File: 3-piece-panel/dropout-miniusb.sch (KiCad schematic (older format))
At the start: 47 parts, among them SW1 Rotary_Encoder_Switch, SW2 SW_Push, U1 ProMicro

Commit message: 3 piece panelization
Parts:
- H1, H2, H3, H4, H5: footprint MountingHole:MountingHole_2.2mm_M2_Pad -> MountingHole:MountingHole_3.7mm
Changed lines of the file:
@@
 F 0 "H2" H 7900 2196 50  0000 L CNN
 F 1 "MountingHole" H 7900 2105 50  0000 L CNN
-F 2 "MountingHole:MountingHole_2.2mm_M2_Pad" H 7800 2150 50  0001 C CNN
+F 2 "MountingHole:MountingHole_3.7mm" H 7800 2150 50  0001 C CNN
 F 3 "~" H 7800 2150 50  0001 C CNN
 	1    7800 2150
@@
 F 0 "H3" H 7900 2546 50  0000 L CNN
 F 1 "MountingHole" H 7900 2455 50  0000 L CNN
-F 2 "MountingHole:MountingHole_2.2mm_M2_Pad" H 7800 2500 50  0001 C CNN
+F 2 "MountingHole:MountingHole_3.7mm" H 7800 2500 50  0001 C CNN
 F 3 "~" H 7800 2500 50  0001 C CNN
 	1    7800 2500
@@
 F 0 "H4" H 7900 2896 50  0000 L CNN
 F 1 "MountingHole" H 7900 2805 50  0000 L CNN
-F 2 "MountingHole:MountingHole_2.2mm_M2_Pad" H 7800 2850 50  0001 C CNN
+F 2 "MountingHole:MountingHole_3.7mm" H 7800 2850 50  0001 C CNN
 F 3 "~" H 7800 2850 50  0001 C CNN
 	1    7800 2850
@@
 F 0 "H5" H 7900 3246 50  0000 L CNN
 F 1 "MountingHole" H 7900 3155 50  0000 L CNN
-F 2 "MountingHole:MountingHole_2.2mm_M2_Pad" H 7800 3200 50  0001 C CNN
+F 2 "MountingHole:MountingHole_3.7mm" H 7800 3200 50  0001 C CNN
 F 3 "~" H 7800 3200 50  0001 C CNN
 	1    7800 3200
@@
 F 0 "H1" H 7900 1896 50  0000 L CNN
 F 1 "MountingHole" H 7900 1805 50  0000 L CNN
-F 2 "MountingHole:MountingHole_2.2mm_M2_Pad" H 7800 1850 50  0001 C CNN
+F 2 "MountingHole:MountingHole_3.7mm" H 7800 1850 50  0001 C CNN
 F 3 "~" H 7800 1850 50  0001 C CNN
 	1    7800 1850

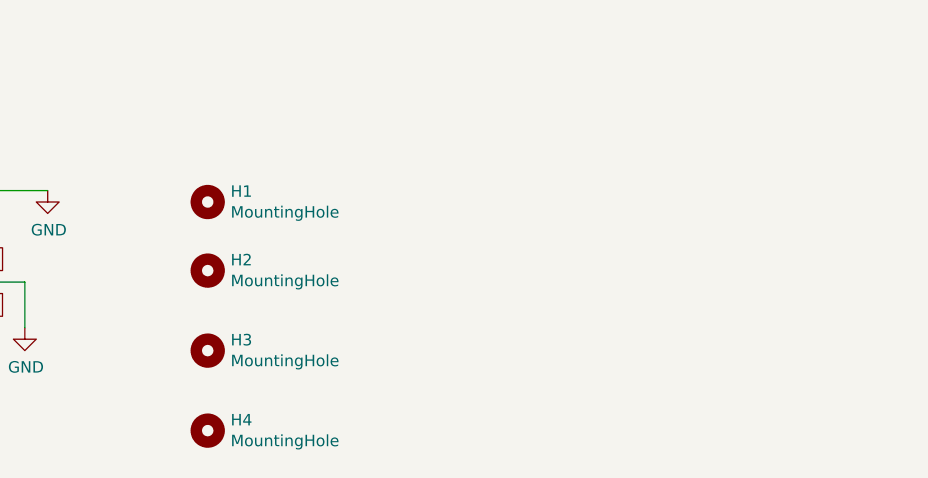
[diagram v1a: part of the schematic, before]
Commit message: adding copper plated mounting holes
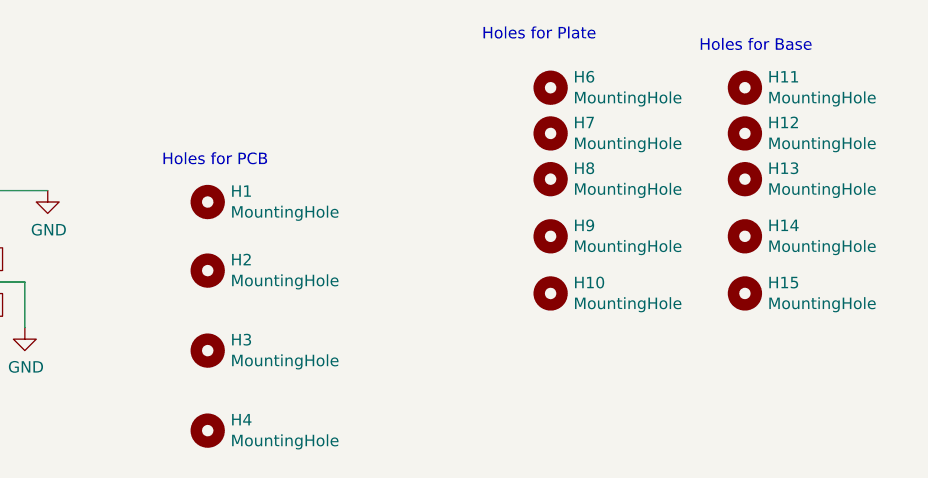
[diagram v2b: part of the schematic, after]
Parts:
- added H10, H11, H12, H13, H14, H15, H6, H7, H8, H9: MountingHole, MountingHole:MountingHole_2.2mm_M2_Pad, symbol Mechanical:MountingHole
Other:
- note added: "Holes for Base"
- note added: "Holes for PCB"
- note added: "Holes for Plate"
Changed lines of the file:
@@
 Wire Wire Line
 	8350 4050 8850 4050
-$Comp
-L power:GND #PWR08
-U 1 1 5FD00893
-P 9300 3750
-F 0 "#PWR08" H 9300 3500 50  0001 C CNN
-F 1 "GND" H 9305 3577 50  0000 C CNN
-F 2 "" H 9300 3750 50  0001 C CNN
-F 3 "" H 9300 3750 50  0001 C CNN
-	1    9300 3750
-	1    0    0    -1
-$EndComp
 Wire Wire Line
 	8850 4050 8850 3900
@@
 	1    0    0    -1
 $EndComp
-Connection ~ 9000 3750
-Wire Wire Line
-	9000 3750 9300 3750
 NoConn ~ 8350 4650
 Wire Wire Line
@@
 Wire Wire Line
 	6550 1800 7100 1800
+$Comp
+L Mechanical:MountingHole H6
+U 1 1 5FCEF804
+P 9300 1350
+F 0 "H6" H 9400 1396 50  0000 L CNN
+F 1 "MountingHole" H 9400 1305 50  0000 L CNN
+F 2 "MountingHole:MountingHole_2.2mm_M2_Pad" H 9300 1350 50  0001 C CNN
+F 3 "~" H 9300 1350 50  0001 C CNN
+	1    9300 1350
+	1    0    0    -1
+$EndComp
+$Comp
+L Mechanical:MountingHole H7
+U 1 1 5FCEFF4E
+P 9300 1550
+F 0 "H7" H 9400 1596 50  0000 L CNN
+F 1 "MountingHole" H 9400 1505 50  0000 L CNN
+F 2 "MountingHole:MountingHole_2.2mm_M2_Pad" H 9300 1550 50  0001 C CNN
+F 3 "~" H 9300 1550 50  0001 C CNN
+	1    9300 1550
+	1    0    0    -1
+$EndComp
+$Comp
+L Mechanical:MountingHole H8
+U 1 1 5FCF347A
+P 9300 1750
+F 0 "H8" H 9400 1796 50  0000 L CNN
+F 1 "MountingHole" H 9400 1705 50  0000 L CNN
+F 2 "MountingHole:MountingHole_2.2mm_M2_Pad" H 9300 1750 50  0001 C CNN
+F 3 "~" H 9300 1750 50  0001 C CNN
+	1    9300 1750
+	1    0    0    -1
+$EndComp
+$Comp
+L Mechanical:MountingHole H9
+U 1 1 5FCF6A76
+P 9300 2000
+F 0 "H9" H 9400 2046 50  0000 L CNN
+F 1 "MountingHole" H 9400 1955 50  0000 L CNN
+F 2 "MountingHole:MountingHole_2.2mm_M2_Pad" H 9300 2000 50  0001 C CNN
+F 3 "~" H 9300 2000 50  0001 C CNN
+	1    9300 2000
+	1    0    0    -1
+$EndComp
+$Comp
+L Mechanical:MountingHole H10
+U 1 1 5FCF9F59
+P 9300 2250
+F 0 "H10" H 9400 2296 50  0000 L CNN
+F 1 "MountingHole" H 9400 2205 50  0000 L CNN
+F 2 "MountingHole:MountingHole_2.2mm_M2_Pad" H 9300 2250 50  0001 C CNN
+F 3 "~" H 9300 2250 50  0001 C CNN
+	1    9300 2250
+	1    0    0    -1
+$EndComp
+$Comp
+L Mechanical:MountingHole H11
+U 1 1 5FCFE769
+P 10150 1350
+F 0 "H11" H 10250 1396 50  0000 L CNN
+F 1 "MountingHole" H 10250 1305 50  0000 L CNN
+F 2 "MountingHole:MountingHole_2.2mm_M2_Pad" H 10150 1350 50  0001 C CNN
+F 3 "~" H 10150 1350 50  0001 C CNN
+	1    10150 1350
+	1    0    0    -1
+$EndComp
+$Comp
+L Mechanical:MountingHole H12
+U 1 1 5FCFE76F
+P 10150 1550
+F 0 "H12" H 10250 1596 50  0000 L CNN
+F 1 "MountingHole" H 10250 1505 50  0000 L CNN
+F 2 "MountingHole:MountingHole_2.2mm_M2_Pad" H 10150 1550 50  0001 C CNN
+F 3 "~" H 10150 1550 50  0001 C CNN
+	1    10150 1550
+	1    0    0    -1
+$EndComp
+$Comp
+L Mechanical:MountingHole H13
+U 1 1 5FCFE775
+P 10150 1750
+F 0 "H13" H 10250 1796 50  0000 L CNN
+F 1 "MountingHole" H 10250 1705 50  0000 L CNN
+F 2 "MountingHole:MountingHole_2.2mm_M2_Pad" H 10150 1750 50  0001 C CNN
+F 3 "~" H 10150 1750 50  0001 C CNN
+	1    10150 1750
+	1    0    0    -1
+$EndComp
+$Comp
+L Mechanical:MountingHole H14
+U 1 1 5FCFE77B
+P 10150 2000
+F 0 "H14" H 10250 2046 50  0000 L CNN
+F 1 "MountingHole" H 10250 1955 50  0000 L CNN
+F 2 "MountingHole:MountingHole_2.2mm_M2_Pad" H 10150 2000 50  0001 C CNN
+F 3 "~" H 10150 2000 50  0001 C CNN
+	1    10150 2000
+	1    0    0    -1
+$EndComp
+$Comp
+L Mechanical:MountingHole H15
+U 1 1 5FCFE781
+P 10150 2250
+F 0 "H15" H 10250 2296 50  0000 L CNN
+F 1 "MountingHole" H 10250 2205 50  0000 L CNN
+F 2 "MountingHole:MountingHole_2.2mm_M2_Pad" H 10150 2250 50  0001 C CNN
+F 3 "~" H 10150 2250 50  0001 C CNN
+	1    10150 2250
+	1    0    0    -1
+$EndComp
+Connection ~ 9000 3750
+Wire Wire Line
+	9000 3750 9300 3750
+$Comp
+L power:GND #PWR08
+U 1 1 5FD00893
+P 9300 3750
+F 0 "#PWR08" H 9300 3500 50  0001 C CNN
+F 1 "GND" H 9305 3577 50  0000 C CNN
+F 2 "" H 9300 3750 50  0001 C CNN
+F 3 "" H 9300 3750 50  0001 C CNN
+	1    9300 3750
+	1    0    0    -1
+$EndComp
+Text Notes 7600 1700 0    50   ~ 0
+Holes for PCB
+Text Notes 9000 1150 0    50   ~ 0
+Holes for Plate
+Text Notes 9950 1200 0    50   ~ 0
+Holes for Base
 $EndSCHEMATC

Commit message: rev 0.4
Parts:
- added U2: ProMicro, promicro:ProMicro, symbol promicro:ProMicro
- H10, H11, H12, H13, H14, H15, H6, H7, H8, H9: footprint MountingHole:MountingHole_2.2mm_M2_Pad -> MountingHole:MountingHole_2.2mm_M2
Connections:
- net COL0: now also U1.10 (E6), U2.10 (E6); no longer J-ISP1.1 (Pin_1), U1.15 (B3)
- net COL1: now also U1.9 (D7), U2.9 (D7); no longer J-ISP1.3 (Pin_3), U1.16 (B1)
- net COL2: now also J-ISP1.3 (Pin_3), U1.16 (B1), U2.16 (B1); no longer U1.9 (D7)
- net COL3: now also U1.17 (F7), U2.17 (F7); no longer U1.8 (C6)
- net GND: now also U2.23 (GND), U2.3 (GND), U2.4 (GND)
- net NUMLED: now also U1.12 (B5), U2.12 (B5); no longer U1.13 (B6)
- net RESET: now also U2.22 (RST)
- net ROT-A: now also U1.19 (F5), U2.19 (F5); no longer U1.6 (SDA)
- net ROT-B: now also U1.18 (F6), U2.18 (F6); no longer U1.7 (D4)
- net ROW0: now also U1.20 (F4), U2.20 (F4); no longer U1.5 (SCL)
- net ROW1: now also U1.11 (B4), U2.11 (B4); no longer J-ISP1.4 (Pin_4), U1.14 (B2)
- net ROW2: now also J-ISP1.1 (Pin_1), U1.15 (B3), U2.15 (B3); no longer U1.10 (E6)
- net ROW3: now also J-ISP1.4 (Pin_4), U1.14 (B2), U2.14 (B2); no longer U1.11 (B4)
- net ROW4: now also U1.13 (B6), U2.13 (B6); no longer U1.12 (B5)
- net VCC: now also U2.21 (VCC)
- no-connect marks 7 -> 14
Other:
- note added: "micro-usb\n"
- note added: "mini-usb\n"
- moved on the sheet: J-ISP1, SW2, U1

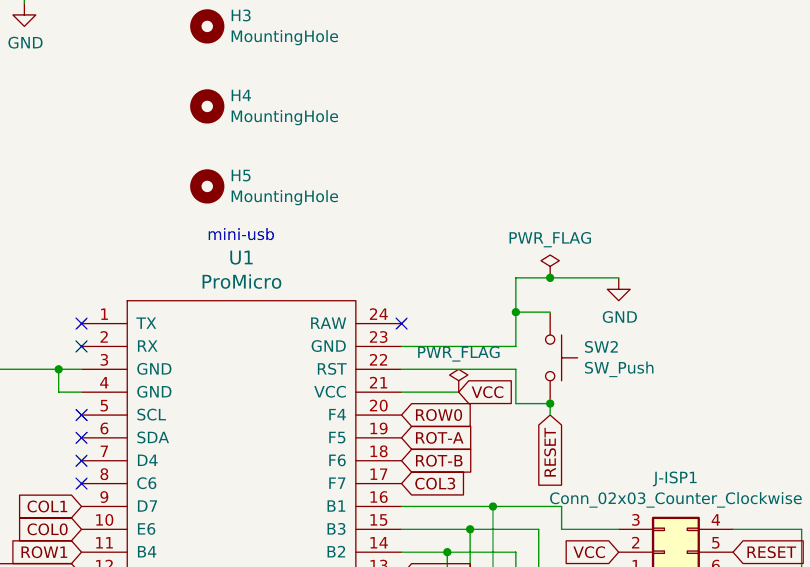
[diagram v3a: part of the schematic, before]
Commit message: qmk backlight numlock
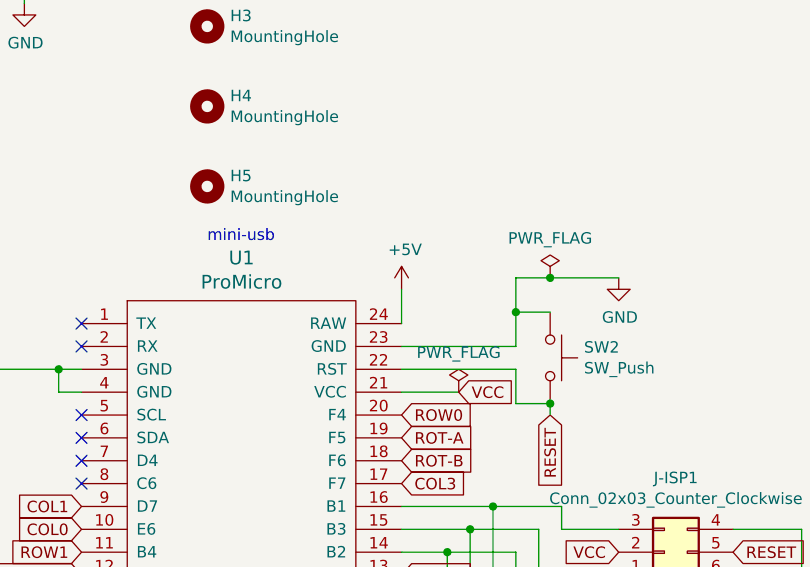
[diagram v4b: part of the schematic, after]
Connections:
- net +5V: now reaches U1.24 (RAW)
- no-connect marks 14 -> 13
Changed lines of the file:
@@
 Wire Wire Line
 	3000 2050 3000 2300
-$Comp
-L power:GND #PWR01
-U 1 1 5FC8A443
-P 3000 2300
-F 0 "#PWR01" H 3000 2050 50  0001 C CNN
-F 1 "GND" H 3005 2127 50  0000 C CNN
-F 2 "" H 3000 2300 50  0001 C CNN
-F 3 "" H 3000 2300 50  0001 C CNN
-	1    3000 2300
-	1    0    0    -1
-$EndComp
 Wire Wire Line
 	3900 2100 3900 2300
@@
 Text Notes 7800 3450 0    50   ~ 0
 mini-usb\n
-NoConn ~ 8650 3800
 Wire Wire Line
 	9150 3900 9150 3750
@@
 Wire Wire Line
 	8650 4100 8900 4100
+$Comp
+L power:+5V #PWR0106
+U 1 1 5FF0E2E0
+P 8650 3650
+F 0 "#PWR0106" H 8650 3500 50  0001 C CNN
+F 1 "+5V" H 8665 3823 50  0000 C CNN
+F 2 "" H 8650 3650 50  0001 C CNN
+F 3 "" H 8650 3650 50  0001 C CNN
+	1    8650 3650
+	1    0    0    -1
+$EndComp
+Wire Wire Line
+	8650 3800 8650 3650
+$Comp
+L power:GND #PWR?
+U 1 1 5FF1CEC0
+P 3000 2300
+F 0 "#PWR?" H 3000 2050 50  0001 C CNN
+F 1 "GND" H 3005 2127 50  0000 C CNN
+F 2 "" H 3000 2300 50  0001 C CNN
+F 3 "" H 3000 2300 50  0001 C CNN
+	1    3000 2300
+	1    0    0    -1
+$EndComp
 $EndSCHEMATC
